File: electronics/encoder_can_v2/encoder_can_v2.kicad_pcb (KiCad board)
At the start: 4 copper layers, 19.2 x 42.4 mm, 41 parts, among them J1 5V GND CANH CANL solder pads, J2 SWD pogo, U1 STM32G431KBU6, U2 TMAG5273A2QDBVR, U3 TMAG5273A2QDBVR, U4 TCAN332GDCNR, U5 TPS7A2033PDBVR, Y1 16MHz CL12pF ESR80

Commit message: Add powered 2.54 mm SWD clip interface to V2 encoder
Use five J2 pads for +5V input, GND, SWDIO, SWCLK and NRST. Keep Hall positions and the PCB outline unchanged, document J1/J2 and clip wiring, and include the current KiCad manufacturing and review package.

Validation: native and portable ERC/DRC and schematic parity passed; 13 generator tests passed; three enclosure intersection probes are empty.
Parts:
- J2: value SWD pogo -> SWD pogo P2.54; footprint Encoder_CAN:SWD_Pogo_1x05 -> Encoder_CAN:SWD_Pogo_1x05_P2.54mm
- moved J2 27.4 mm to (118.8, 80.0), turned to 136.8 degrees
- moved FIDF1 2.05 mm to (116.0, 83.7)
- moved FIDB1 1.47 mm to (117.9, 84.1)
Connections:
- J2 pad 1: +3V3 -> +5V
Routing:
- net NRST: track 20.4 -> 37.7 mm, vias 3 -> 4
- net +5V: track 29.9 -> 46.8 mm, vias 2 -> 3
- net +3V3: track 68.0 -> 65.4 mm
- net GND: track 27.2 -> 28.1 mm, vias 18 -> 19
- net SWDIO: track 21.3 -> 20.9 mm, vias 3 -> 0
- net SWCLK: track 20.2 -> 20.5 mm, vias 2 -> 3

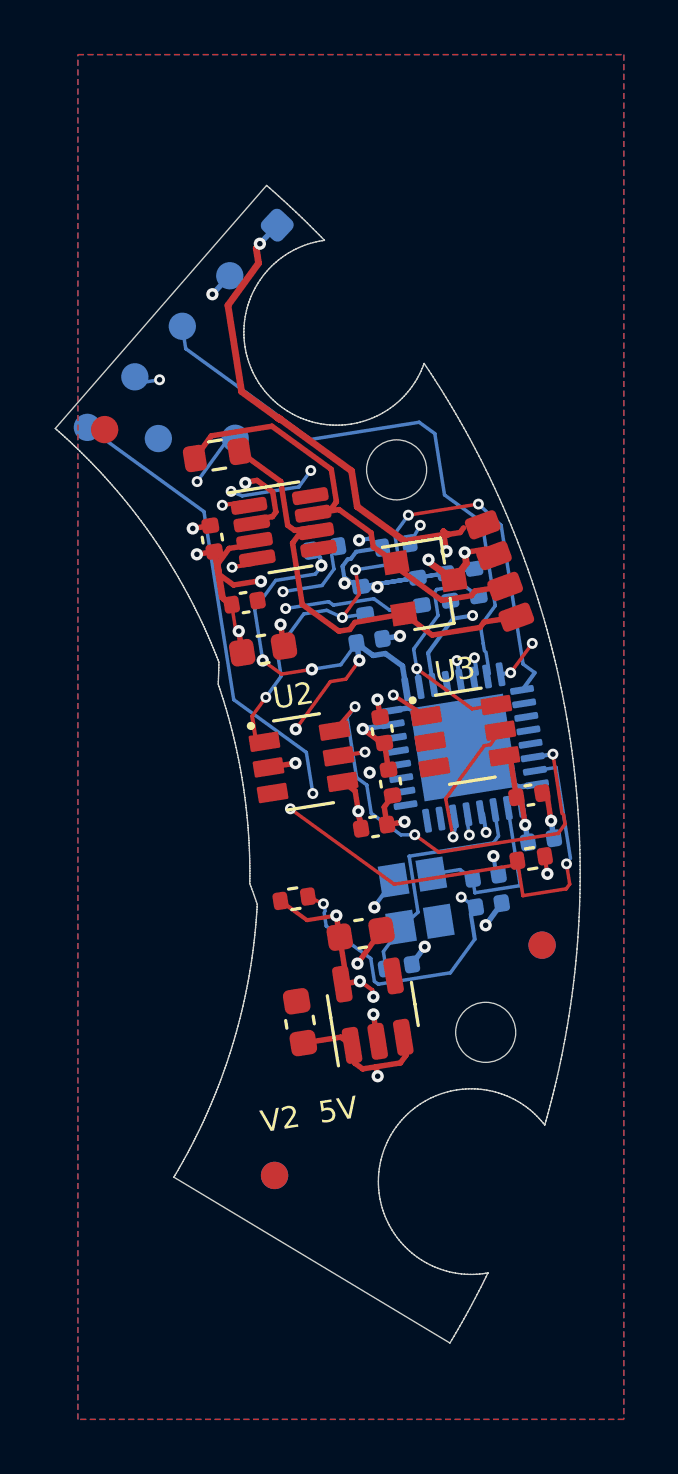
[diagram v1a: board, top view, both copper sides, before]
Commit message: Save CAN encoder V2.4 for D70 reducer geometry
Preserve the narrow four-layer 0.8 mm PCB with fixed Hall positions, 0.5 mm via-to-pad clearance and vias outside component bodies. Record the D70 reducer dimensions and variant identifier explicitly.

Include matching manufacturing files, assembly data, release audits and the mechanical generator integration. Validate with 23 generator tests and zero native ERC, DRC, unconnected and schematic parity errors after unpacking the portable project. Keep ZIP and STL deliverables outside Git.
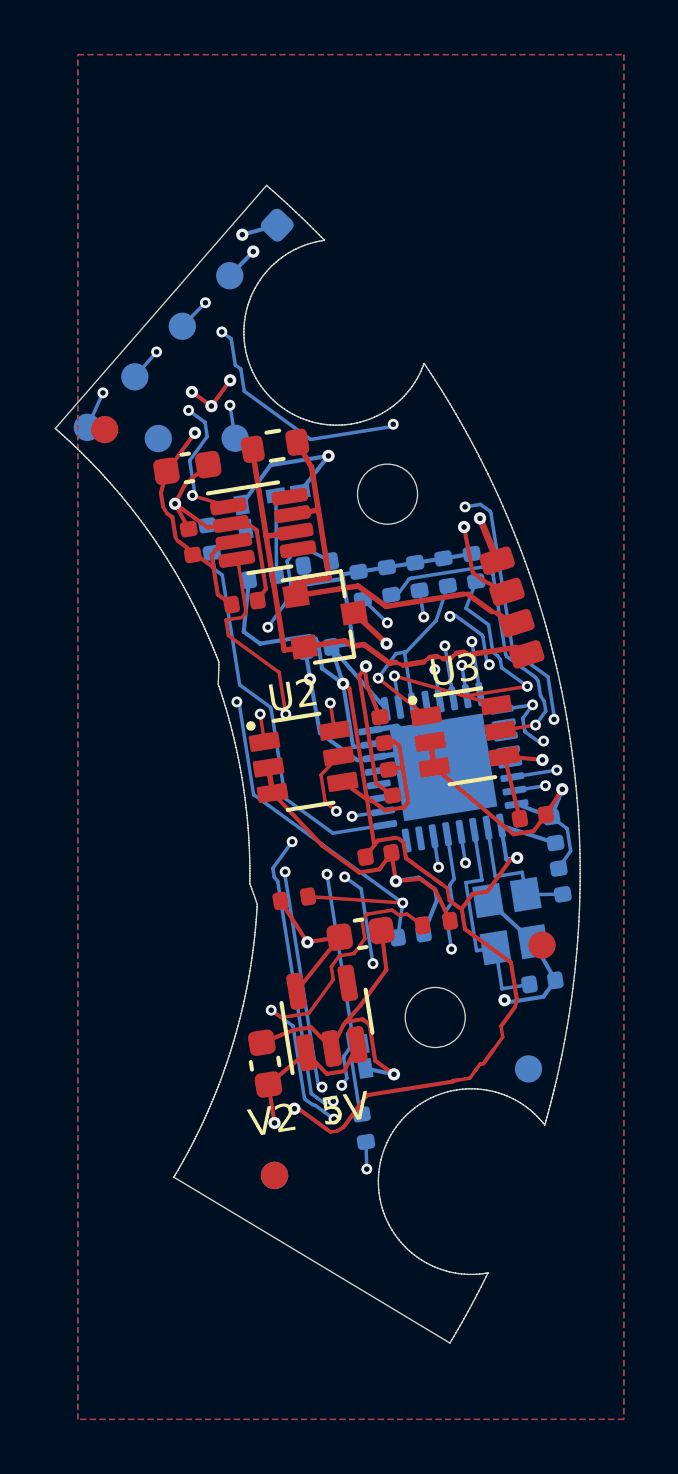
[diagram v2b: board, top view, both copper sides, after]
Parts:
- added D2: LED green, Encoder_CAN:LED_Kingbright_APG1005, B.Cu at (122.7, 86.1)
- added D3: LED yellow, Encoder_CAN:LED_Kingbright_APG1005, B.Cu at (121.1, 86.9)
- added D4: LED red, Encoder_CAN:LED_Kingbright_APG1005, B.Cu at (125.5, 106.7)
- added R10: 1k, Encoder_CAN:R_0402_Status, B.Cu at (121.8, 89.2)
- added R11: 1k, Encoder_CAN:R_0402_Status, B.Cu at (119.8, 87.7)
- added R12: 1k, Encoder_CAN:R_0402_Status, B.Cu at (125.5, 109.3)
- moved C3 7.20 mm to (119.0, 85.1)
- moved C14 5.29 mm to (132.0, 104.0)
- moved FIDB2 4.56 mm to (131.5, 107.2)
- moved R5 4.20 mm to (128.1, 101.8)
- moved D1 3.85 mm to (124.1, 90.6)
- moved Y1 3.54 mm to (130.9, 101.7)
- moved C12 3.07 mm to (127.2, 102.3)
- moved C13 2.76 mm to (132.7, 100.3), turned to 99 degrees
- moved R9 2.15 mm to (122.2, 84.3), turned to -171 degrees
- moved C10 1.98 mm to (121.9, 107.0)
- moved H1 1.93 mm to (128.1, 105.3)
- moved C2 1.90 mm to (123.8, 91.8), turned to -171 degrees
- moved U5 1.70 mm to (124.1, 105.3)
- moved J1 1.41 mm to (130.9, 90.3), turned to 17.5 degrees
- moved R8 1.33 mm to (126.4, 89.3), turned to -81 degrees
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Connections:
- U1 pad 10: unconnected-(U1-PA5-Pad10) -> LED_PHASE
- U1 pad 9: unconnected-(U1-PA4-Pad9) -> LED_CMD
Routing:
- net GND: track 28.1 -> 79.9 mm, vias 19 -> 11
- net BOOT0: track 32.5 -> 69.4 mm, vias 3 -> 6
- net +3V3: track 65.4 -> 89.0 mm, vias 17 -> 6
- net I2C1_SDA: track 24.6 -> 46.7 mm, vias 4 -> 5
- net I2C1_SCL: track 23.0 -> 42.5 mm, vias 5 -> 6
- net LED_PHASE: track 0.00 -> 17.6 mm, vias 0 -> 4
- net INT_INNER: track 18.3 -> 35.2 mm, vias 3 -> 5
- net LED_CMD: track 0.00 -> 13.9 mm
- net CAN_RX: track 12.8 -> 25.3 mm
- net +5V: track 46.8 -> 58.3 mm, vias 3 -> 6
- net SWCLK: track 20.5 -> 31.0 mm, vias 3 -> 4
- net CAN_TX: track 13.3 -> 20.3 mm, vias 2 -> 3
- net INT_OUTER: track 31.4 -> 25.6 mm, vias 4 -> 2
- net NRST: track 37.7 -> 34.2 mm
- net I2C2_SCL: track 12.0 -> 8.62 mm, vias 2 -> 1
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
